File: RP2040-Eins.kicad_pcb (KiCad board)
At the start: 2 copper layers, 68.6 x 53.3 mm, 55 parts, among them J1 CONN_PWR, J10 CONN_USB, J2 CONN_ICSP, J3 CONN_A, J4 CONN_P, J5 CONN_X, J7 CONN_JTAG, J8 CONN_D1, J9 CONN_D2, Q1 AO3401A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

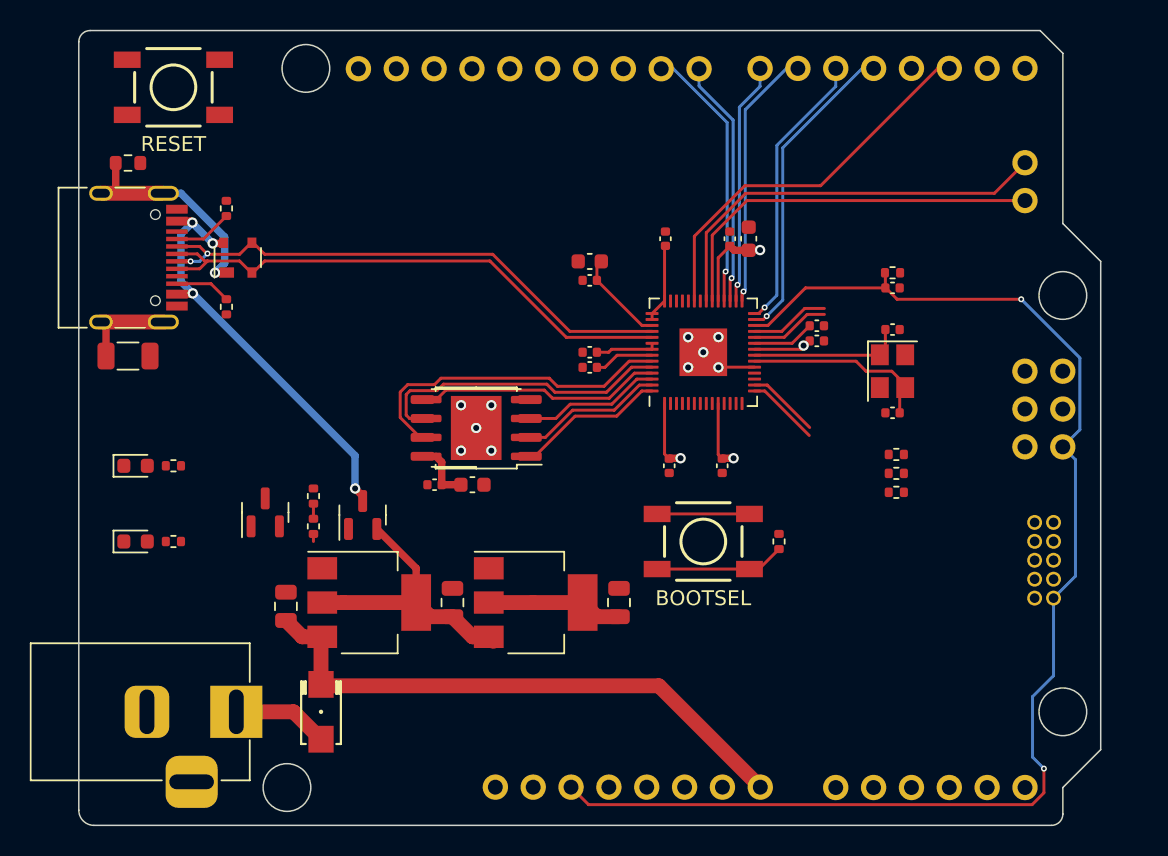
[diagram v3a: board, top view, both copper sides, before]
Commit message: Added ferrite beads. Changed power routing.
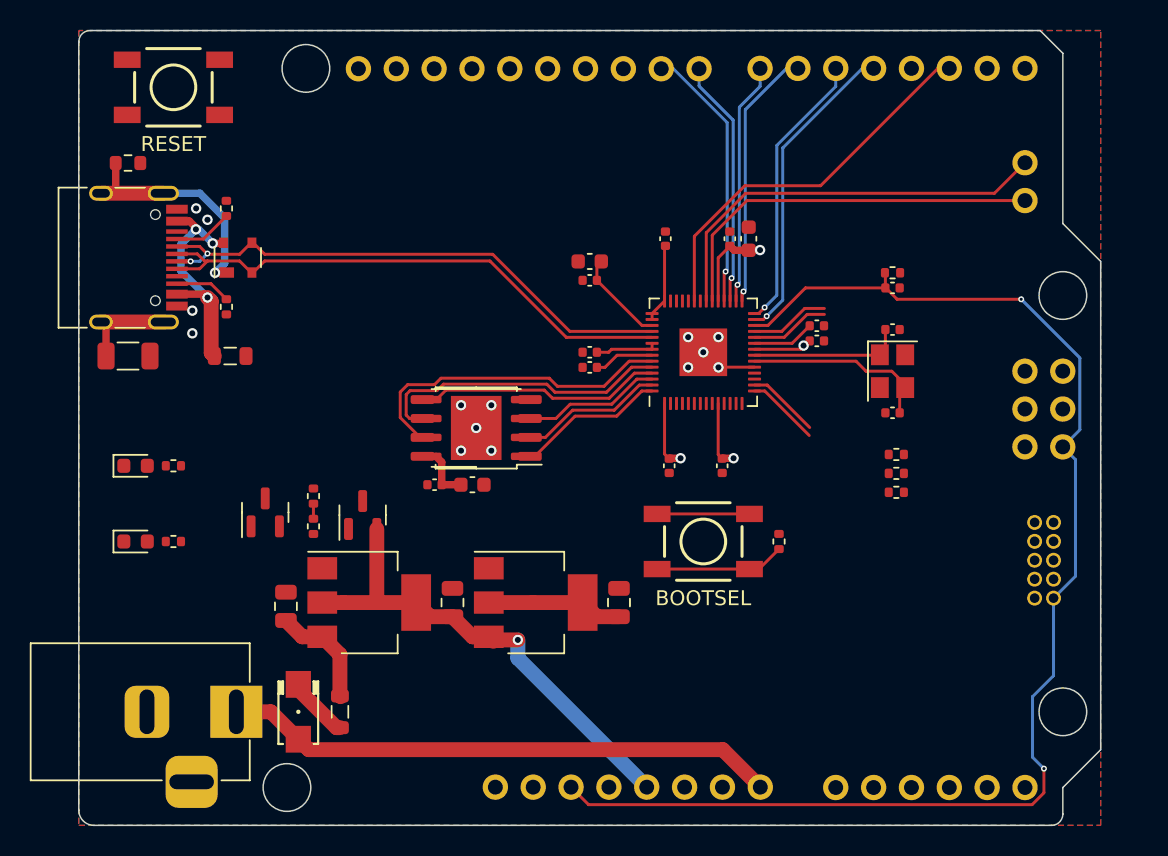
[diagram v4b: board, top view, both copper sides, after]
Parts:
- added FB1: 100@100MHz, Inductor_SMD:L_0805_2012Metric, F.Cu at (144.5, 119.4)
- added FB2: 100@100MHz, Inductor_SMD:L_0805_2012Metric, F.Cu at (137.2, 95.5)
- moved D5 1.52 mm to (141.7, 119.4)
- turned R1 to 0 degrees
- turned R6 to 180 degrees
- turned SW2 to 180 degrees
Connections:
- C12 pad 1: VIN -> VPWR
- D5 pad 1: VIN -> Net-(D5-K)
- D5 pad 2: Net-(D5-A) -> VIN
- J1 pad 1: Net-(D5-A) -> VIN
- Q1 pad 3: VBUS -> VUSB
- R8 pad 1: VIN -> VPWR
- U3 pad 3: VIN -> VPWR
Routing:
- net +5V: track 18.6 -> 33.0 mm, vias 0 -> 1
- net VBUS: track 28.9 -> 15.8 mm, vias 4 -> 3
- net VPWR: track 0.00 -> 7.42 mm
- net Net-(D5-A): track 6.09 -> 0.00 mm
- net Net-(D5-K): track 0.00 -> 4.19 mm
- net VIN: track 39.0 -> 37.3 mm
- net SHIELD: track 22.4 -> 23.1 mm
- net GND: vias 10 -> 14
- added copper zone on B.Cu, net GND
- added copper zone on F.Cu, net GND

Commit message: Added few traces
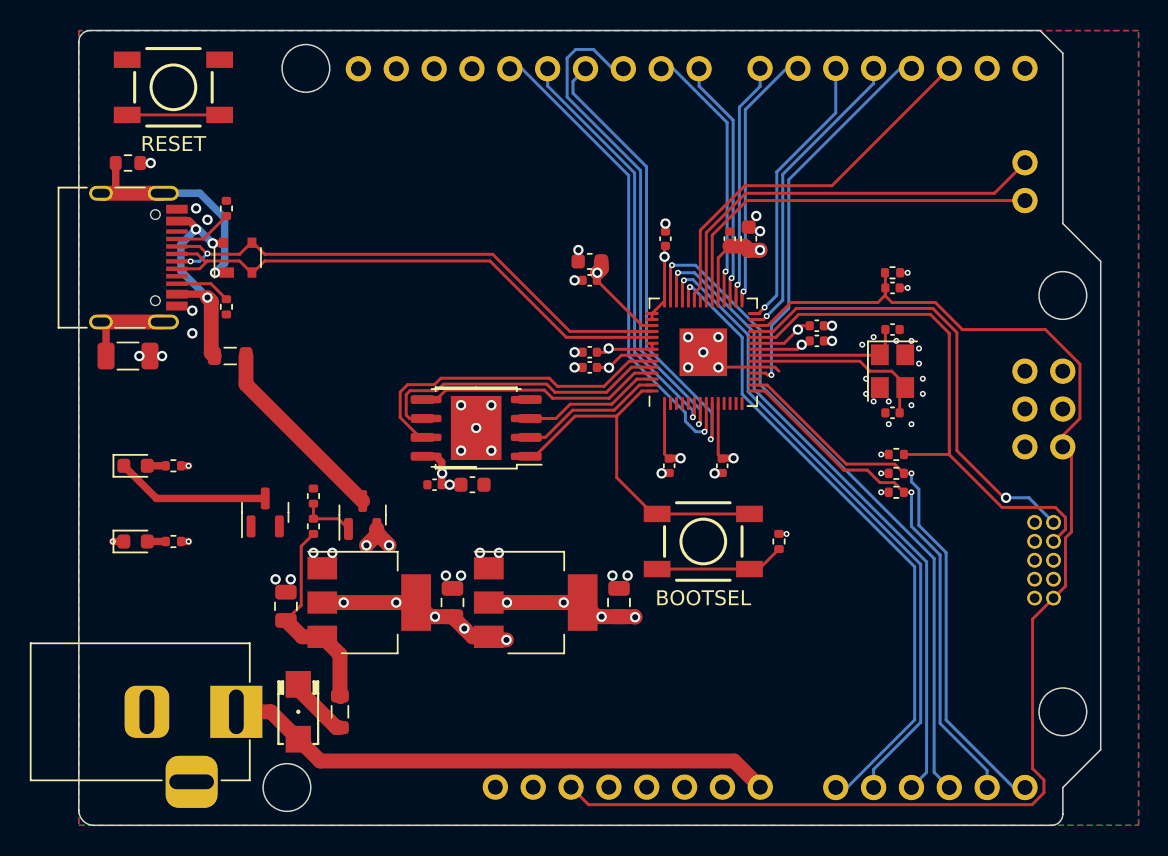
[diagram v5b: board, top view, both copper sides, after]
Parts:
- moved R2 2.54 mm to (181.9, 102.1)
- moved R4 2.54 mm to (181.9, 104.6)
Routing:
- net D17_A3: track 0.00 -> 46.1 mm, vias 0 -> 1
- net D16_A2: track 0.00 -> 44.5 mm, vias 0 -> 1
- net D15_A1: track 0.00 -> 43.8 mm, vias 0 -> 1
- net D14_A0: track 0.00 -> 43.5 mm, vias 0 -> 1
- net +5V: track 33.0 -> 73.7 mm, vias 1 -> 7
- net D10_SS: track 0.00 -> 34.3 mm, vias 0 -> 1
- net D19_SCL: track 4.88 -> 37.7 mm, vias 0 -> 1
- net D13_SCK: track 0.00 -> 32.5 mm, vias 0 -> 1
- net SWCLK: track 5.33 -> 36.9 mm
- net D11_MOSI: track 0.00 -> 31.6 mm, vias 0 -> 1
- net D18_SDA: track 4.91 -> 35.3 mm, vias 0 -> 1
- net D12_MISO: track 0.00 -> 28.4 mm, vias 0 -> 1
- net D3: track 0.00 -> 26.1 mm, vias 0 -> 1
- net SWD: track 5.33 -> 31.3 mm, vias 0 -> 1
- net +1V1: track 14.6 -> 37.0 mm, vias 0 -> 3
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- added copper zone on In2.Cu, net +3V3
- added copper zone on In2.Cu, net +5V
- added copper zone on In1.Cu, net GND
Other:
- copper layers 2 -> 4

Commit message: Added few traces
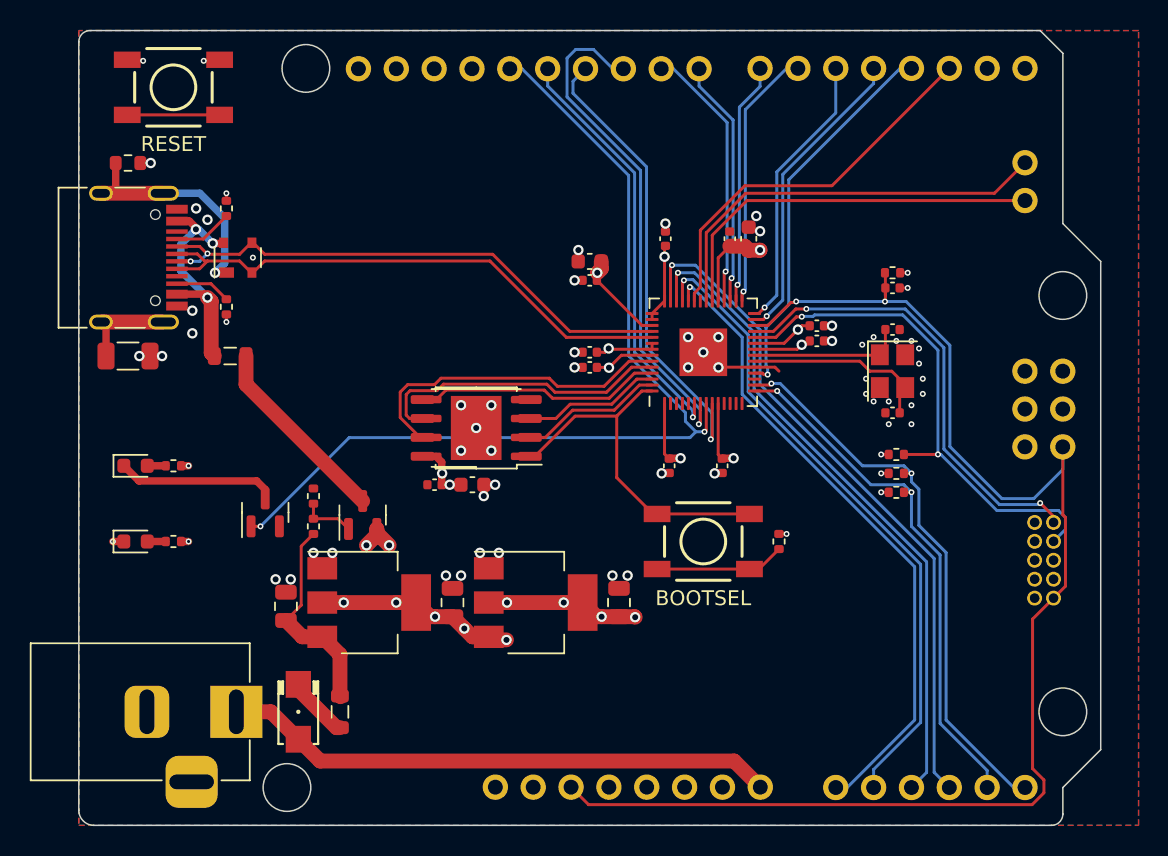
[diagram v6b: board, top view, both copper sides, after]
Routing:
- net D13_SCK: track 32.5 -> 65.0 mm, vias 1 -> 2
- net GND: track 5.96 -> 10.7 mm, vias 56 -> 63
- net RESET: track 96.3 -> 98.9 mm, vias 0 -> 2
- net SWCLK: track 36.9 -> 35.4 mm, vias 0 -> 2
- net D19_SCL: track 37.7 -> 38.3 mm, vias 1 -> 2
- net D18_SDA: track 35.3 -> 35.8 mm, vias 1 -> 2
- net SWD: track 31.3 -> 30.9 mm, vias 1 -> 2

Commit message: Moved stuff around
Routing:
- added copper zone on F.Cu, net SHIELD
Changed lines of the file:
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@@
   (segment (start 188.448 84.582) (end 190.5 82.53) (width 0.2) (layer "F.Cu") (net 30))
   (segment (start 171.75806 84.582) (end 188.448 84.582) (width 0.2) (layer "F.Cu") (net 30))
-  (segment (start 136.0975 95.504) (end 135.886 95.2925) (width 1) (layer "F.Cu") (net 31))
-  (segment (start 135.886 91.826) (end 135.636 91.576) (width 1) (layer "F.Cu") (net 31))
   (segment (start 134.420498 86.45) (end 133.585 86.45) (width 0.5) (layer "F.Cu") (net 31))
   (segment (start 136.67345 87.94455) (end 136.718 87.9) (width 0.5) (layer "F.Cu") (net 31))
   (segment (start 135.636 91.576) (end 135.41 91.35) (width 0.5) (layer "F.Cu") (net 31))
+  (segment (start 136.0975 95.504) (end 135.886 95.2925) (width 1) (layer "F.Cu") (net 31))
   (segment (start 135.41 91.35) (end 133.585 91.35) (width 0.5) (layer "F.Cu") (net 31))
   (segment (start 135.987982 87.94455) (end 136.67345 87.94455) (width 0.5) (layer "F.Cu") (net 31))
+  (segment (start 135.886 95.2925) (end 135.886 91.826) (width 1) (layer "F.Cu") (net 31))
   (segment (start 134.859502 86.889004) (end 134.420498 86.45) (width 0.5) (layer "F.Cu") (net 31))
-  (segment (start 135.886 95.2925) (end 135.886 91.826) (width 1) (layer "F.Cu") (net 31))
+  (segment (start 135.886 91.826) (end 135.636 91.576) (width 1) (layer "F.Cu") (net 31))
   (segment (start 134.859502 87.0005) (end 134.859502 86.889004) (width 0.5) (layer "F.Cu") (net 31))
   (via (at 134.859502 87.0005) (size 0.7) (drill 0.4) (layers "F.Cu" "B.Cu") (net 31))
@@
   (segment (start 140.901 113.251) (end 141.997 114.347) (width 1) (layer "F.Cu") (net 67))
   (segment (start 144.5725 118.364) (end 144.526 118.3175) (width 1) (layer "F.Cu") (net 67))
+  (zone (net 59) (net_name "SHIELD") (layer "F.Cu") (hatch edge 0.5)
+    (priority 3)
+    (connect_pads yes (clearance 0.3))
+    (min_thickness 0.25) (filled_areas_thickness no)
+    (fill yes (thermal_gap 0.5) (thermal_bridge_width 0.5))
+    (polygon
+      (pts
+        (xy 124.46 84.074)
+        (xy 132.842 84.074)
+        (xy 132.842 93.726)
+        (xy 124.46 93.726)
+      )
+    )
+  )
   (zone (net 4) (net_name "GND") (layers "F.Cu" "In1.Cu" "B.Cu") (hatch edge 0.5)
     (connect_pads yes (clearance 0.3))

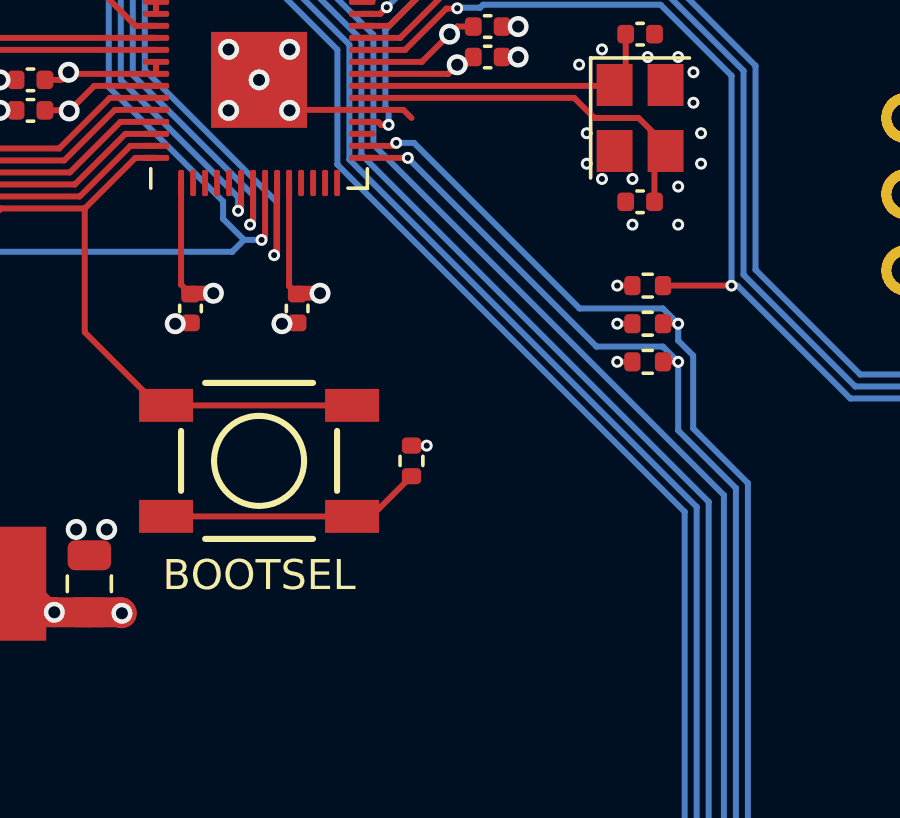
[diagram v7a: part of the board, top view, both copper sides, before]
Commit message: Added RGB LED
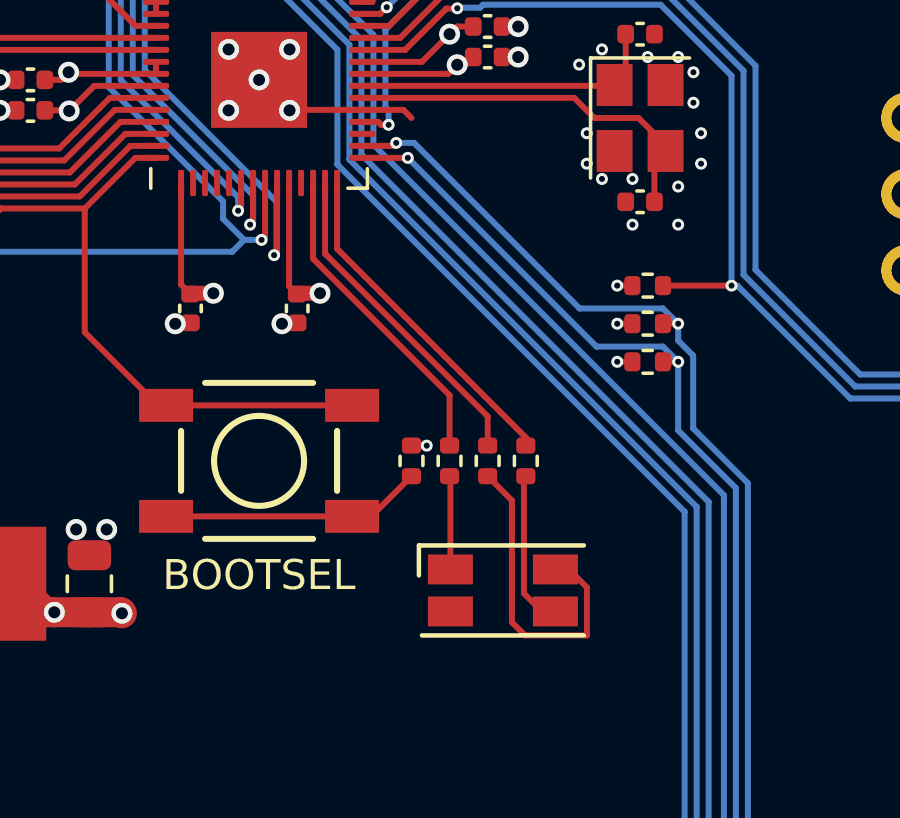
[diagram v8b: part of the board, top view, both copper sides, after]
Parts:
- added D4: XL-3227RGB-RF, LED_SMD:LED_RGB_1210, F.Cu at (177.0, 112.3)
- added R13: 5k1, Resistor_SMD:R_0402_1005Metric, F.Cu at (175.3, 108.0)
- added R14: 5k1, Resistor_SMD:R_0402_1005Metric, F.Cu at (176.5, 108.0)
- added R15: 5k1, Resistor_SMD:R_0402_1005Metric, F.Cu at (177.8, 108.0)
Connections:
- U2 pad 12: unconnected-(U2-GPIO9-Pad12) -> LED_R
- U2 pad 13: unconnected-(U2-GPIO10-Pad13) -> LED_G
- U2 pad 14: unconnected-(U2-GPIO11-Pad14) -> LED_B
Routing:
- net LED_B: track 0.00 -> 11.4 mm
- net LED_G: track 0.00 -> 11.0 mm
- net Net-(D4-GK): track 0.00 -> 10.8 mm
- net LED_R: track 0.00 -> 10.6 mm
- net Net-(D4-BK): track 0.00 -> 5.23 mm
- net Net-(D4-RK): track 0.00 -> 3.12 mm
